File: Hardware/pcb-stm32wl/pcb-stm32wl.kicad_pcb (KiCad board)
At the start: 4 copper layers, 40.9 x 67.7 mm, 166 parts, among them J1 Debug, J2 U.FL-R-SMT-1, J3 Grove_I2C, Q1 SI2323DS, Q2 2SC4213, SW1 SW_Push, SW2 RESET, U1 TPS22917DBV, U10 NX3L1T3157GM, U11 BGS13S4N9, U12 NX3L1T3157GM, U2 RP605Z283B, U3 TPS22917DBV, U4 TPS22917DBV, U5 MX25R1635, U6 LIS2DH12, U7 SHTC3, U8 ATECC608A-TNGLORAU, U9 STM32WLxx_QFN48, X1 32MHz, X2 32.768KHz

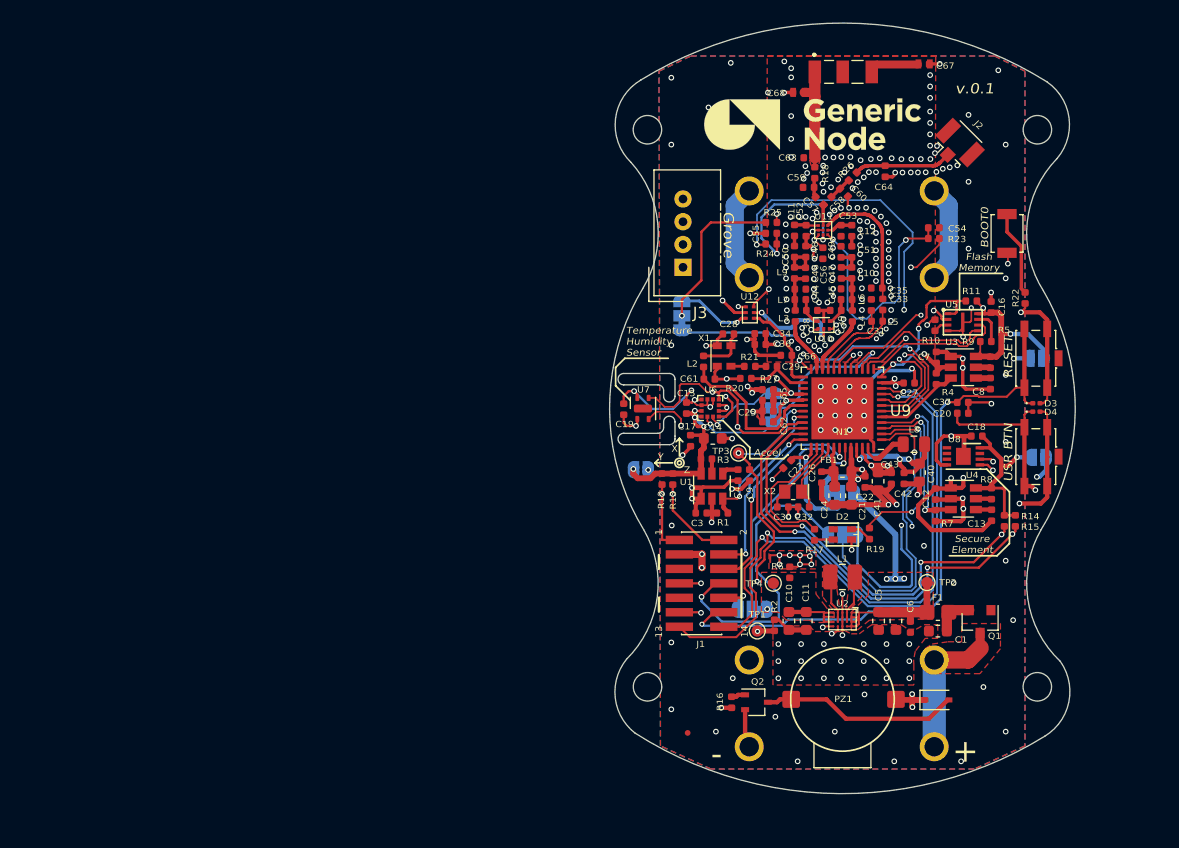
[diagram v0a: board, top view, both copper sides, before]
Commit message: pcb,sch: Add V0.2 HW design with external battery holder
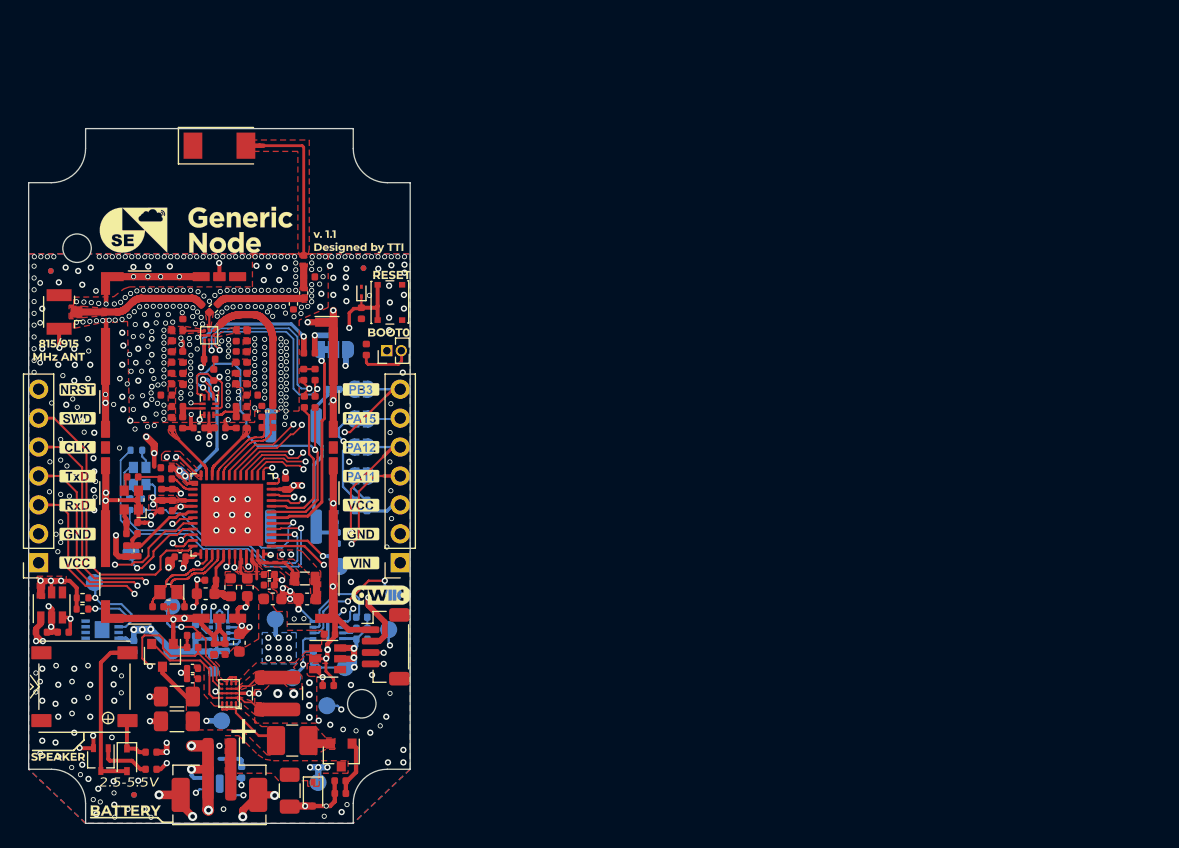
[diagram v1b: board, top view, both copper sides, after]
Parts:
- removed BH1, BH3: Battery_Cell+, node-lib-v1:BAT_BK-92
- removed BH2, BH4: Battery_Cell-, node-lib-v1:BAT_BK-92
- removed C51, C66: 33pF, Capacitor_SMD:C_0402_1005Metric
- removed C52: 2.7pF, Capacitor_SMD:C_0402_1005Metric
- removed C53: 1.3pF, Capacitor_SMD:C_0402_1005Metric
- removed C56: 1nF, Capacitor_SMD:C_0402_1005Metric
- removed C67: 5.0pF, Capacitor_SMD:C_0402_1005Metric
- removed C68: 3.6pF, Capacitor_SMD:C_0402_1005Metric
- removed G***: LOGO, node-lib-v1:qr_azerimaker_11mm
- removed G*** (x2): LOGO, node-lib-v1:Icon_Battery_1000px
- removed G*** (x2): LOGO, node-lib-v1:Logo_GN-4000px
- removed H3, H4: MountingHole, MountingHole:MountingHole_2.5mm
- removed JP10: BOOT0, Button_Switch_SMD:SW_SPST_B3U-1000P
- removed JP11: VDD_RF_SW, Jumper:SolderJumper-3_P1.3mm_Bridged12_RoundedPad1.0x1.5mm_NumberLabels
- removed JP7: VBAT, Jumper:SolderJumper-3_P1.3mm_Bridged12_RoundedPad1.0x1.5mm_NumberLabels
- removed JP8: SWO, Jumper:SolderJumper-3_P1.3mm_Bridged12_RoundedPad1.0x1.5mm_NumberLabels
- removed JP9: INT, Jumper:SolderJumper-3_P1.3mm_Bridged12_RoundedPad1.0x1.5mm_NumberLabels
- removed R25: 100R, Resistor_SMD:R_0402_1005Metric
- removed R26, R27: 0R, Resistor_SMD:R_0402_1005Metric
- removed the REF** at (139.7, 95.5)
- removed the REF** at (147.8, 95.5)
- removed U12: NX3L1T3157GM, node-lib-v1:6-XFDFN_SOT-886
- removed X2: 32.768KHz, node-lib-v1:Crystal_SMD_NX2012SA_32.768KHz
- added D5: ESD9D5V, Diode_SMD:D_SOD-923, F.Cu at (97.5, 88.8)
- added FID2: Fiducial, Fiducial:Fiducial_0.5mm_Mask1.5mm, B.Cu at (77.5, 133.0)
- added FID3: Fiducial, Fiducial:Fiducial_0.5mm_Mask1.5mm, F.Cu at (70.2, 87.0)
- added FID4: Fiducial, Fiducial:Fiducial_0.5mm_Mask1.5mm, B.Cu at (70.2, 87.0)
- added FID5: Fiducial, Fiducial:Fiducial_0.5mm_Mask1.5mm, F.Cu at (97.7, 86.8)
- added FID6: Fiducial, Fiducial:Fiducial_0.5mm_Mask1.5mm, B.Cu at (97.7, 86.8)
- added G-ACCELL: LOGO, node-lib-v1:LAbel_ACCELL_2000px, B.Cu at (83.1, 123.0)
- added G-ANT: LOGO, node-lib-v1:Label_ANT, F.Cu at (71.0, 93.9)
- added G-BAT: LOGO, node-lib-v1:Label_BATTERY_2500px, F.Cu at (76.7, 134.3)
- added G-BOOT0: LOGO, node-lib-v1:Label_BOOT0_4000px, F.Cu at (99.8, 92.3)
- added G-CLK: LOGO, node-lib-v1:PinName_CLK, F.Cu at (72.6, 102.5)
- added G-FLASH: LOGO, node-lib-v1:Label_FLASH_3000px, B.Cu at (92.3, 115.1)
- added G-GND: LOGO, node-lib-v1:PinName_GND, F.Cu at (97.4, 110.1)
- added G-GND2: LOGO, node-lib-v1:PinName_GND, F.Cu at (72.6, 110.1)
- added G-Logo: LOGO, node-lib-v1:Logo_GN-SE-4500px, F.Cu at (83.0, 83.4)
- added G-NRST: LOGO, node-lib-v1:PinName_NRST, F.Cu at (72.6, 97.4)
- added G-PA11: LOGO, node-lib-v1:PinName_PA11, F.Cu at (97.4, 105.0)
- added G-PA12: LOGO, node-lib-v1:PinName_PA12, F.Cu at (97.4, 102.5)
- added G-PA15: LOGO, node-lib-v1:PinName_PA15, F.Cu at (97.4, 99.9)
- added G-PB3: LOGO, node-lib-v1:PinName_PB3, F.Cu at (97.4, 97.4)
- added G-QWIIC: LOGO, node-lib-v1:Logo_qwiic_4000px, F.Cu at (99.2, 115.4)
- added G-RST: LOGO, node-lib-v1:Label_RESET_4000px, F.Cu at (100.1, 87.3)
- added G-RXD: LOGO, node-lib-v1:PinName_RxD, F.Cu at (72.6, 107.5)
- added G-SE: LOGO, node-lib-v1:Label_SE_3000px, B.Cu at (77.0, 115.0)
- added G-SPKR: LOGO, node-lib-v1:Label_Speaker, F.Cu at (70.9, 129.6)
- added G-SWD: LOGO, node-lib-v1:PinName_SWD, F.Cu at (72.6, 99.9)
- added G-TH: LOGO, node-lib-v1:Label_T_H_2000px, B.Cu at (90.0, 128.8)
- added G-TXD: LOGO, node-lib-v1:PinName_TxD, F.Cu at (72.6, 105.0)
- added G-VCC: LOGO, node-lib-v1:PinName_VCC, F.Cu at (97.4, 107.5)
- added G-VCC2: LOGO, node-lib-v1:PinName_VCC, F.Cu at (72.5, 112.6)
- added G-VIN: LOGO, node-lib-v1:PinName_VIN, F.Cu at (97.4, 112.6)
- added G-version: LOGO, node-lib-v1:Logo_design_version_2000px, F.Cu at (97.5, 84.2)
- added J10: Qwiic, Connector_JST:JST_SH_BM04B-SRSS-TB_1x04-1MP_P1.00mm_Vertical, F.Cu at (99.6, 120.0)
- added J4: RF_Shield_One_Piece, node-lib-v1:RF_Shield_SnapOn_30x20mm_w_Cutout_n_GND_Pads, F.Cu at (85.0, 102.5)
- added J5: S1001-46R, node-lib-v1:RF_Shield_Clip_S1001-46R, F.Cu at (85.0, 117.5)
- added J6: S1001-46R, node-lib-v1:RF_Shield_Clip_S1001-46R, F.Cu at (95.0, 102.5)
- added J7: U.FL/iPEX, Connector_Coaxial:U.FL_Hirose_U.FL-R-SMT-1_Vertical, F.Cu at (71.4, 90.6)
- added J8: DEBUG, Connector_PinSocket_2.54mm:PinSocket_1x07_P2.54mm_Vertical, F.Cu at (69.1, 112.6)
- added J9: UART/I2C, Connector_PinSocket_2.54mm:PinSocket_1x07_P2.54mm_Vertical, F.Cu at (100.9, 112.6)
- added JP4: SCL2_CUT, Jumper:SolderJumper-2_P1.3mm_Bridged2Bar_RoundedPad1.0x1.5mm, B.Cu at (97.4, 102.5)
- added JP5: BOOT0, Connector_PinHeader_1.27mm:PinHeader_1x02_P1.27mm_Vertical, F.Cu at (99.7, 94.0)
- added L13: 23nH, Inductor_SMD:L_0402_1005Metric, F.Cu at (92.4, 86.1)
- added L14: 4.3nH, Inductor_SMD:L_0402_1005Metric, F.Cu at (92.9, 87.5)
- added REF**: FabDrawing-4Layer, node-lib-v1:PCBStackup_FabDrawing-4Layer-Metric, F.Cu at (150.0, 72.5)
- added TP10: VCC_F, TestPoint:TestPoint_Pad_D1.5mm, B.Cu at (96.0, 121.8)
- added TP11: VCC_S, TestPoint:TestPoint_Pad_D1.5mm, B.Cu at (80.8, 120.4)
- added TP12: SDA, TestPoint:TestPoint_Pad_D1.5mm, B.Cu at (77.2, 111.7)
- added TP13: SCL, TestPoint:TestPoint_Pad_D1.5mm, B.Cu at (74.0, 114.4)
- added TP5: VCC, TestPoint:TestPoint_Pad_D1.5mm, B.Cu at (89.9, 117.6)
- added TP6: CS, TestPoint:TestPoint_Pad_D1.5mm, B.Cu at (91.4, 122.7)
- added TP7: MISO, TestPoint:TestPoint_Pad_D1.5mm, B.Cu at (100.3, 115.4)
- added TP8: SCK, TestPoint:TestPoint_Pad_D1.5mm, B.Cu at (94.4, 125.2)
- added TP9: MOSI, TestPoint:TestPoint_Pad_D1.5mm, B.Cu at (99.9, 118.5)
- added Y1: 32.768KHz, node-lib-v1:Crystal_SMD_NX2012SA_32.768KHz, F.Cu at (80.5, 115.2)
- AE1: value ANT_M620720 -> NN02-201; footprint node-lib-v1:ANT_M620720 -> node-lib-v1:Antenna_Fractus_NN02-201
- C1: value 10uF -> 100uF; footprint Capacitor_SMD:C_0603_1608Metric -> Capacitor_SMD:C_1206_3216Metric
- C10: value DNM -> 100nF; footprint Capacitor_SMD:C_0603_1608Metric -> Capacitor_SMD:C_0402_1005Metric
- C11: value 22uF -> 1uF; footprint Capacitor_SMD:C_0603_1608Metric -> Capacitor_SMD:C_0402_1005Metric
- C12: value 1uF -> 22uF; footprint Capacitor_SMD:C_0402_1005Metric -> Capacitor_SMD:C_0603_1608Metric
- C13: value DNM -> 4.7uF; footprint Capacitor_SMD:C_0402_1005Metric -> Capacitor_SMD:C_0603_1608Metric
- C14: value 10uF -> 100nF; footprint Capacitor_SMD:C_0603_1608Metric -> Capacitor_SMD:C_0402_1005Metric
- C15, C27: value 100nF -> 4.7uF; footprint Capacitor_SMD:C_0402_1005Metric -> Capacitor_SMD:C_0603_1608Metric
- C19, C22, C42: value 100nF -> 33pF
- C2: value 10uF -> 10nF; footprint Capacitor_SMD:C_0603_1608Metric -> Capacitor_SMD:C_0402_1005Metric
- C20: value DNM -> 100nF
- C21, C41: value 4.7uF -> 33pF; footprint Capacitor_SMD:C_0603_1608Metric -> Capacitor_SMD:C_0402_1005Metric
- C23: value 100nF -> 47pF
- C24: value 4.7uF -> 100nF; footprint Capacitor_SMD:C_0603_1608Metric -> Capacitor_SMD:C_0402_1005Metric
- C25: value 100nF -> 47nF
- C26: value 100nF -> 68pF
- C28: value 10nF -> 470nF; footprint Capacitor_SMD:C_0402_1005Metric -> Capacitor_SMD:C_0603_1608Metric
- C29: value 1nF -> 100nF
- C30, C44: value 6.8pF -> 2.7pF
- C31: value 2.7pF -> 3.6pF
- C32: value 6.8pF -> 33pF
- C33: value 3.6pF -> 33pF
- C34: value 47nF -> 10nF
- C35: value DNM -> 5.6pF
- C36: value 68nF -> 6.8pF
- C37: value 100nF -> 2.7pF
- C38: value 33pF -> 2.4pF
- C39: value 33pF -> 3.3pF
- C4: value DNM -> 100uF; footprint Capacitor_SMD:C_0402_1005Metric -> Capacitor_SMD:C_1206_3216Metric
- C40: value 470nF -> 3.9pF; footprint Capacitor_SMD:C_0603_1608Metric -> Capacitor_SMD:C_0402_1005Metric
- C43: value 100nF -> 1nF
- C45: value 5.6pF -> 1.3pF
- C46: value 2.4pF -> 5.6pF
- C47: value 2.7pF -> 1nF
- C48: value 3.9pF -> 1nF
- C49: value 3.3pF -> 5.6pF
- C5: value 4.7uF -> 100uF; footprint Capacitor_SMD:C_0603_1608Metric -> Capacitor_SMD:C_1206_3216Metric
- C50: value 33pF -> 1nF
- C54: value 1nF -> 3.3pF
- C55: value 1nF -> DNM
- C57, C65: value 33pF -> 100nF
- C58: value DNM -> 10uF; footprint Capacitor_SMD:C_0402_1005Metric -> Capacitor_SMD:C_0603_1608Metric; moved to B.Cu
- C59, C60, C63, C64: value DNM -> 100nF; moved to B.Cu
- C6: value 100nF -> 1uF
- C61, R15, R24: moved to B.Cu
- C62: value 33pF -> 100nF; moved to B.Cu
- C7: value 1uF -> 100nF
- C8: value DNM -> 1uF
- D1: value 1N4148WS -> PESD5V0S1BA
- D2: value EAST1616RGBB2 -> 1N4148WSF-7; footprint node-lib-v1:LED_RGB_0606 -> node-lib-v1:D_SOD-323F_custom
- D3: value ESDALC6V1-1U2 -> FM-B2020RGBA; footprint Diode_SMD:D_0201_0603Metric -> LED_SMD:LED_Cree-PLCC4_2x2mm_CW; moved to B.Cu
- D4: value ESDALC6V1-1U2 -> ESD9D5V; footprint Diode_SMD:D_0201_0603Metric -> Diode_SMD:D_SOD-923; moved to B.Cu
- F1: value PTC 6V 750MA -> PTC 13V 1A; footprint node-lib-v1:Fuse_0805_2012Metric_Castellated -> Fuse:Fuse_1210_3225Metric_Castellated
- J1: value Debug -> S1001-46R; footprint node-lib-v1:PinHeader_2x07_P1.27mm_Vertical_SMD -> node-lib-v1:RF_Shield_Clip_S1001-46R
- J2: value U.FL-R-SMT-1 -> JST-PH; footprint Connector_Coaxial:U.FL_Hirose_U.FL-R-SMT-1_Vertical -> Connector_JST:JST_PH_B2B-PH-SM4-TB_1x02-1MP_P2.00mm_Vertical
- J3: value Grove_I2C -> S1001-46R; footprint Connector:NS-Tech_Grove_1x04_P2mm_Vertical -> node-lib-v1:RF_Shield_Clip_S1001-46R
- JP1: value Sensor_VCC -> VDD_RF_SW; footprint Jumper:SolderJumper-2_P1.3mm_Open_RoundedPad1.0x1.5mm -> Jumper:SolderJumper-3_P1.3mm_Bridged12_RoundedPad1.0x1.5mm_NumberLabels
- JP2: value Flash_VCC -> BUZZ_KILL; footprint Jumper:SolderJumper-2_P1.3mm_Open_RoundedPad1.0x1.5mm -> Jumper:SolderJumper-2_P1.3mm_Bridged2Bar_RoundedPad1.0x1.5mm
- JP3: value Secure_Element_VCC -> SDA2_CUT; footprint Jumper:SolderJumper-2_P1.3mm_Open_RoundedPad1.0x1.5mm -> Jumper:SolderJumper-2_P1.3mm_Bridged2Bar_RoundedPad1.0x1.5mm
- JP6: value JTDI -> BTN_CUT; footprint Jumper:SolderJumper-3_P1.3mm_Bridged12_RoundedPad1.0x1.5mm_NumberLabels -> Jumper:SolderJumper-2_P1.3mm_Bridged2Bar_RoundedPad1.0x1.5mm
- L1: value 2.2 uH -> 2.2uH; footprint Inductor_SMD:L_1008_2520Metric -> node-lib-v1:L_HPC4012TF-2R2M
- L10: value 3.3nH -> 1400R @1GHz
- L2: value 1400R @1GHz -> 3.3nH
- L4: value 3.3nH -> 15uH; footprint Inductor_SMD:L_0402_1005Metric -> node-lib-v1:L_0805_2012Metric_custom
- L8: value 15uH -> 3nH; footprint Inductor_SMD:L_0805_2012Metric -> Inductor_SMD:L_0402_1005Metric
- N1: value NewAge_3inch_round -> BoLink-16174563; footprint node-lib-v1:NewAge_3inch_round -> node-lib-v1:BoLink_704025
- PZ1: value AST0927 2.73kHz 85dB -> MLT-7525; footprint node-lib-v1:Buzzer_AST0927MW-3.6TRQ -> node-lib-v1:Buzzer_MLT-7525
- Q1: value SI2323DS -> CEN2321A
- Q2: value 2SC4213 -> S9013W
- R1: value 100K -> 10K
- R11: value 10K -> DNM; moved to B.Cu
- R12: value 4K7 -> DNM; moved to B.Cu
- R13: value 4K7 -> 10K; moved to B.Cu
- R17: value 330R -> 4K7
- R18: value 0R -> 4K7; moved to B.Cu
- R19: value 100R -> 33R
- R20: value DNM -> 10K
- R21: value 220R -> 1K; footprint Inductor_SMD:L_0402_1005Metric -> Resistor_SMD:R_0402_1005Metric; moved to B.Cu
- R22: value 10K -> 330R; footprint Inductor_SMD:L_0402_1005Metric -> Resistor_SMD:R_0402_1005Metric; moved to B.Cu
- R23: value 100R -> 330R; moved to B.Cu
- R3: value 1K -> 100K
- R5: value 1K -> 220R; footprint Resistor_SMD:R_0402_1005Metric -> Inductor_SMD:L_0402_1005Metric
- R6: value 0R -> 100R
- R7: value 100K -> 100R
- R8: value 1K -> 100R
- R9: value DNM -> 0R
- SW1: value SW_Push -> USR_BTN; footprint node-lib-v1:EVQ-P2R02W -> node-lib-v1:PushButton_KSC721GLFS; moved to B.Cu
- SW2: footprint node-lib-v1:EVQ-P2R02W -> node-lib-v1:SW_SPST_SKSHABE010
- TP1: value VBAT_READ -> VIN; footprint TestPoint:TestPoint_Pad_D1.0mm -> TestPoint:TestPoint_Pad_D1.5mm; moved to B.Cu
- TP2: footprint TestPoint:TestPoint_Pad_D1.0mm -> TestPoint:TestPoint_Pad_D1.5mm; moved to B.Cu
- TP3: value VBAT_ADC -> VBAT_READ_EN; footprint TestPoint:TestPoint_Pad_D1.0mm -> TestPoint:TestPoint_Pad_D1.5mm; moved to B.Cu
- TP4: value VDD -> VBAT_ADC; footprint TestPoint:TestPoint_Pad_D1.0mm -> TestPoint:TestPoint_Pad_D1.5mm; moved to B.Cu
- U10: value NX3L1T3157GM -> SHTC3; footprint node-lib-v1:6-XFDFN_SOT-886 -> node-lib-v1:Sensirion_DFN-4-1EP_2x2mm_P1mm_EP0.7x1.6mm; moved to B.Cu
- U11: value BGS13S4N9 -> ATECC608A-TNGLORA; footprint node-lib-v1:RFSW_BGS13S4N9E6327XTSA1 -> Package_DFN_QFN:DFN-8-1EP_3x2mm_P0.5mm_EP1.3x1.5mm; moved to B.Cu
- U2: value RP605Z283B -> TPS3839G25; footprint node-lib-v1:WLCSP-20-P3_1.994x1.609mm_Layout5x4_P0.4mm -> Package_TO_SOT_SMD:SOT-23
- U4: value TPS22917DBV -> RP605Z283B; footprint Package_TO_SOT_SMD:SOT-23-6 -> node-lib-v1:WLCSP-20-P3_1.994x1.609mm_Layout5x4_P0.4mm
- U5: value MX25R1635 -> STM32WLE5CC; footprint node-lib-v1:FLASH_UFDFN-8-MX25R1635F -> Package_DFN_QFN:QFN-48-1EP_7x7mm_P0.5mm_EP5.45x5.45mm
- U6: value LIS2DH12 -> TS3A5223RSWR; footprint Package_LGA:LGA-12_2x2mm_P0.5mm -> Package_DFN_QFN:UQFN-10_1.4x1.8mm_P0.4mm
- U7: value SHTC3 -> BGS13S4N9; footprint node-lib-v1:Sensirion_DFN-4-1EP_2x2mm_P1mm_EP0.7x1.6mm -> node-lib-v1:RFSW_BGS13S4N9E6327XTSA1
- U8: value ATECC608A-TNGLORAU -> MX25R1635; footprint Package_DFN_QFN:DFN-8-1EP_3x2mm_P0.5mm_EP1.3x1.5mm -> node-lib-v1:FLASH_UFDFN-8-MX25R1635F; moved to B.Cu
- U9: value STM32WLxx_QFN48 -> LIS2DH12; footprint Package_DFN_QFN:QFN-48-1EP_7x7mm_P0.5mm_EP5.45x5.45mm -> Package_LGA:LGA-12_2x2mm_P0.5mm; moved to B.Cu
- X1: footprint node-lib-v1:TCXO_NT2016SA-32M-END4263A -> Crystal:Crystal_SMD_Abracon_ABM10-4Pin_2.5x2.0mm
- moved J2 85.0 mm to (85.0, 131.2), turned to 180 degrees
- moved R14 81.2 mm to (73.0, 115.7), turned to 180 degrees
- moved R22 79.2 mm to (77.7, 102.7), turned to 0 degrees
- moved D3 79.0 mm to (78.0, 105.0), turned to 270 degrees
- moved R5 76.0 mm to (77.4, 105.1), turned to 180 degrees
- moved C16 74.5 mm to (81.5, 112.1), turned to 180 degrees
- moved C63 73.4 mm to (87.0, 131.0), turned to 270 degrees
- moved R23 73.4 mm to (78.2, 107.5), turned to 90 degrees
- moved U11 72.4 mm to (74.7, 118.5), turned to 0 degrees
- moved C18 71.8 mm to (79.9, 106.6), turned to 90 degrees
- moved C7 71.1 mm to (82.6, 122.8), turned to 180 degrees
- moved R9 67.9 mm to (84.5, 90.3), turned to 225 degrees
- moved C58 67.5 mm to (84.5, 121.4), turned to 90 degrees
- moved L10 67.2 mm to (77.3, 110.1), turned to 180 degrees
- moved U4 66.7 mm to (85.8, 124.1), turned to 90 degrees
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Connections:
- AE1 pad 1: Net-(AE1-Pad1) -> (no net)
- C1 pad 2: Net-(C1-Pad2) -> Vin
- C10 pad 2: Net-(C10-Pad2) -> VDDRF
- C11 pad 1: GND -> VDDRF
- C11 pad 2: Net-(C10-Pad2) -> GND
- C12 pad 1: VDD -> GND
- C12 pad 2: GND -> VDDRF
- C13 pad 1: VDD -> VDDRF
- C13 pad 2: Net-(C13-Pad2) -> GND
- C14 pad 1: GND -> VDDRF
- C14 pad 2: /Peripherals/VCC_SENSORS -> GND
- C15 pad 1: GND -> VDDA
- C15 pad 2: /Peripherals/VCC_SENSORS -> GND
- C16 pad 1: GND -> VDDRF
- C16 pad 2: /Peripherals/VCC_FLASH -> GND
- C17 pad 1: GND -> VDDA
- C17 pad 2: /Peripherals/VCC_SENSORS -> GND
- C18 pad 1: GND -> VDDRF
- C18 pad 2: /Peripherals/VCC_SEC_ELM -> GND
- C19 pad 1: GND -> VDDRF
- C19 pad 2: /Peripherals/VCC_SENSORS -> GND
- C2 pad 1: GND -> Net-(C2-Pad1)
- C2 pad 2: +BATT -> GND
- C20 pad 1: GND -> VDDRF
- C20 pad 2: /LoRa MCU/PB3 -> GND
- C21 pad 1: VDD -> VDDPA
- C22 pad 1: VDD -> VDDRF1V55
- C23 pad 1: Net-(C23-Pad1) -> PB0_VDD_TCXO
- C24 pad 1: VDDA -> PB0_VDD_TCXO
- C25 pad 1: VDDRF -> GND
- C25 pad 2: GND -> Net-(C25-Pad2)
- C26 pad 1: VDDA -> Net-(C25-Pad2)
- C27 pad 1: VDD -> VDDRF
- C28 pad 1: GND -> VDDRF1V55
- C28 pad 2: Net-(C28-Pad2) -> GND
- C29 pad 1: Net-(C29-Pad1) -> VDDRF
- C29 pad 2: OSC_IN -> GND
- C3 pad 1: VDD -> VDDRF
- C30 pad 2: OSC32_IN -> /LoRa MCU/RFI_N
- C31 pad 1: GND -> /LoRa MCU/RFI_P
- C32 pad 2: OSC32_OUT -> Net-(C32-Pad2)
- C33 pad 1: /LoRa MCU/RFI_P -> Net-(C33-Pad1)
- C33 pad 2: Net-(C33-Pad2) -> GND
- C35 pad 1: Net-(C33-Pad2) -> GND
- C35 pad 2: GND -> Net-(C35-Pad2)
- C36 pad 1: Net-(C34-Pad2) -> GND
- C36 pad 2: GND -> Net-(C36-Pad2)
- C37 pad 1: GND -> Net-(C35-Pad2)
- C37 pad 2: NRST -> Net-(C37-Pad2)
- C38 pad 1: GND -> Net-(C36-Pad2)
- C39 pad 1: Net-(C39-Pad1) -> GND
- C39 pad 2: GND -> Net-(C37-Pad2)
- C4 pad 1: VDD -> GND
- C4 pad 2: Net-(C4-Pad2) -> +BATT
- C40 pad 1: VDDRF1V55 -> GND
- C40 pad 2: GND -> Net-(C38-Pad2)
- C41 pad 1: VDDRF -> Net-(C38-Pad2)
- C41 pad 2: GND -> Net-(C41-Pad2)
- C42 pad 1: VDDRF1V55 -> Net-(C37-Pad2)
- C42 pad 2: GND -> Net-(C42-Pad2)
- C43 pad 1: VDDRF -> Net-(C43-Pad1)
- C43 pad 2: GND -> OSC_IN
- C46 pad 1: Net-(C44-Pad2) -> GND
- C46 pad 2: Net-(C46-Pad2) -> OSC32_IN
- C47 pad 1: Net-(C45-Pad2) -> GND
- C48 pad 2: Net-(C46-Pad2) -> Net-(C48-Pad2)
- C49 pad 2: Net-(C47-Pad2) -> OSC32_OUT
- C5 pad 1: +BATT -> GND
- C5 pad 2: GND -> +BATT
- C50 pad 1: Net-(C46-Pad2) -> GND
- C54 pad 1: GND -> Net-(C54-Pad1)
- C55 pad 2: Net-(C55-Pad2) -> Net-(C54-Pad2)
- C57 pad 1: Net-(C57-Pad1) -> VDDRF
- C57 pad 2: Net-(C57-Pad2) -> GND
- C58 pad 1: Net-(C57-Pad1) -> GND
- C58 pad 2: Net-(C58-Pad2) -> /Peripherals/VCC_SENSORS
- C59 pad 2: Net-(C57-Pad2) -> /Peripherals/VCC_SENSORS
- C60 pad 2: Net-(C58-Pad2) -> /Peripherals/VCC_FLASH
- C61 pad 1: PB0_VDD_TCXO -> GND
- C61 pad 2: GND -> /Peripherals/VCC_SENSORS
- C62 pad 1: VDDRF1V55 -> GND
- C62 pad 2: GND -> /Peripherals/VCC_SENSORS
- C63 pad 2: Net-(AE1-Pad1) -> /Peripherals/VCC_SENSORS
- C65 pad 1: VDDRF -> GND
- C65 pad 2: GND -> /LoRa MCU/NRST
- C7 pad 1: VDD -> +BATT
- C8 pad 1: VDD -> VDDRF
- C8 pad 2: Net-(C8-Pad2) -> GND
- D1 pad 1: VDD -> Vin
- D1 pad 2: Net-(D1-Pad2) -> GND
- D3 pad 1: NRST -> Net-(D3-Pad1)
- D3 pad 2: GND -> Net-(D3-Pad2)
- D4 pad 1: /LoRa MCU/PB3 -> Net-(C64-Pad2)
- F1 pad 2: Net-(C1-Pad2) -> Net-(F1-Pad2)
- FB1 pad 2: VDD -> VDDRF
- J1 pad 1: /LoRa MCU/I2C1_SDA -> GND
- J2 pad 1: Net-(C64-Pad2) -> Vin
- J3 pad 1: /LoRa MCU/I2C1_SCL -> GND
- JP1 pad 1: VDD -> FE_CTRL3
- JP1 pad 2: /Peripherals/VCC_SENSORS -> Net-(JP1-Pad2)
- JP2 pad 1: VDD -> /LoRa MCU/PA15
- JP2 pad 2: /Peripherals/VCC_FLASH -> Net-(JP2-Pad2)
- JP3 pad 1: VDD -> Net-(JP3-Pad1)
- JP3 pad 2: /Peripherals/VCC_SEC_ELM -> /LoRa MCU/PA11_SDA2
- JP6 pad 1: /Peripherals/BUZZER -> /LoRa MCU/PB3
- L10 pad 1: Net-(C45-Pad2) -> PB0_VDD_TCXO
- L10 pad 2: Net-(C47-Pad2) -> Net-(C34-Pad2)
- L11 pad 1: Net-(C50-Pad2) -> Net-(C41-Pad2)
- L11 pad 2: Net-(C52-Pad2) -> Net-(C44-Pad2)
- L12 pad 1: Net-(C51-Pad2) -> Net-(C42-Pad2)
- L12 pad 2: Net-(C53-Pad2) -> Net-(C45-Pad2)
- L2 pad 1: PB0_VDD_TCXO -> Net-(L2-Pad1)
- L2 pad 2: Net-(C28-Pad2) -> Net-(C35-Pad2)
- L3 pad 2: Net-(C44-Pad2) -> Net-(C36-Pad2)
- L4 pad 1: Net-(L4-Pad1) -> VLXSMPS
- L4 pad 2: Net-(C45-Pad2) -> VDDRF1V55
- L5 pad 1: Net-(C31-Pad2) -> /LoRa MCU/RFI_N
- L6 pad 1: Net-(C39-Pad1) -> Net-(C32-Pad2)
- L6 pad 2: Net-(C45-Pad2) -> Net-(C36-Pad2)
- L7 pad 1: Net-(C38-Pad2) -> Net-(C33-Pad1)
- L7 pad 2: Net-(C44-Pad2) -> Net-(C35-Pad2)
- L8 pad 1: VLXSMPS -> Net-(C35-Pad2)
- L8 pad 2: VDDRF1V55 -> Net-(C37-Pad2)
- L9 pad 1: Net-(C44-Pad2) -> Net-(C36-Pad2)
- L9 pad 2: Net-(C46-Pad2) -> Net-(C38-Pad2)
- PZ1 pad 1: VDD -> Net-(D2-Pad1)
- PZ1 pad 2: Net-(D1-Pad2) -> Net-(D2-Pad2)
- Q1 pad 1: GND -> Net-(C2-Pad1)
- Q1 pad 2: Net-(C1-Pad2) -> Net-(F1-Pad2)
- Q1 pad 3: Net-(BH1-Pad1) -> Vin
- Q2 pad 3: Net-(D1-Pad2) -> Net-(D2-Pad2)
- R1 pad 2: /LoRa MCU/PB12 -> Net-(C2-Pad1)
- R10 pad 1: /Peripherals/VCC_FLASH -> Net-(J7-Pad1)
- R11 pad 2: /Peripherals/FlashCS -> Net-(R11-Pad2)
- R12 pad 1: /LoRa MCU/I2C1_SDA -> /Peripherals/VCC_FLASH
- R12 pad 2: /Peripherals/VCC_SENSORS -> Net-(R12-Pad2)
- R13 pad 1: /Peripherals/VCC_SENSORS -> /Peripherals/VCC_FLASH
- R13 pad 2: /LoRa MCU/I2C1_SCL -> /Peripherals/FlashCS
- R14 pad 1: /LoRa MCU/I2C2_SCL -> /LoRa MCU/PA09_SCL1
- R14 pad 2: /Peripherals/VCC_SEC_ELM -> /Peripherals/VCC_SENSORS
- R15 pad 1: /Peripherals/VCC_SEC_ELM -> Net-(JP3-Pad1)
- R15 pad 2: /LoRa MCU/I2C2_SDA -> VDDRF
- R16 pad 1: /Peripherals/BUZZER -> Net-(JP2-Pad2)
- R17 pad 1: Net-(D2-Pad1) -> /Peripherals/VCC_SENSORS
- R17 pad 2: /Peripherals/LED_R -> /LoRa MCU/PA10_SDA1
- R18 pad 1: Net-(AE1-Pad1) -> VDDRF
- R18 pad 2: Net-(C57-Pad2) -> Net-(JP4-Pad1)
- R19 pad 1: Net-(D2-Pad3) -> VDDRF
- R19 pad 2: /Peripherals/LED_B -> Net-(D2-Pad1)
- R2 pad 2: /LoRa MCU/PB4 -> /Power Supply/LS1_SENSORS_EN
- R20 pad 1: OSC_IN -> GND
- R20 pad 2: GND -> /LoRa MCU/BOOT0
- R21 pad 1: Net-(C29-Pad1) -> /LoRa MCU/PB5
- R21 pad 2: Net-(R21-Pad2) -> Net-(D3-Pad1)
- R22 pad 1: GND -> /LoRa MCU/PB6
- R22 pad 2: Net-(JP10-Pad2) -> Net-(D3-Pad4)
- R23 pad 1: Net-(C54-Pad2) -> /LoRa MCU/PB7
- R23 pad 2: FE_CTRL1 -> Net-(D3-Pad2)
- R24 pad 1: Net-(C55-Pad2) -> Net-(JP6-Pad2)
- R24 pad 2: FE_CTRL2 -> Net-(C64-Pad2)
- R3 pad 1: /Peripherals/VCC_SENSORS -> GND
- R3 pad 2: Net-(R3-Pad2) -> /LoRa MCU/PB4
- R4 pad 2: /LoRa MCU/PB7 -> /Power Supply/LS2_FLASH_EN
- R5 pad 1: /Peripherals/VCC_FLASH -> Net-(C43-Pad1)
- R6 pad 1: Net-(C10-Pad2) -> Net-(C47-Pad2)
- R6 pad 2: VDD -> FE_CTRL2
- R7 pad 1: GND -> Net-(C48-Pad2)
- R7 pad 2: /LoRa MCU/PB6 -> FE_CTRL1
- R8 pad 1: /Peripherals/VCC_SEC_ELM -> Net-(JP1-Pad2)
- R8 pad 2: Net-(R8-Pad2) -> Net-(C50-Pad2)
- R9 pad 1: /Peripherals/VCC_FLASH -> Net-(C54-Pad2)
- R9 pad 2: Net-(R9-Pad2) -> Net-(R10-Pad2)
- SW1 pad 1: GND -> Net-(C64-Pad2)
- SW1 pad 2: /LoRa MCU/PB3 -> GND
- SW2 pad 2: NRST -> /LoRa MCU/NRST
- TP1 pad 1: /LoRa MCU/PB4 -> Vin
- TP3 pad 1: /LoRa MCU/PB2 -> /LoRa MCU/PB4
- TP4 pad 1: Net-(C10-Pad2) -> /LoRa MCU/PB2
- U1 pad 1: VDD -> VDDRF
- U1 pad 3: /LoRa MCU/PB12 -> /Power Supply/LS1_SENSORS_EN
- U1 pad 4: Net-(C4-Pad2) -> (no net)
- U1 pad 5: Net-(R3-Pad2) -> /Peripherals/VCC_SENSORS
- U10 pad 1: Net-(C39-Pad1) -> /Peripherals/VCC_SENSORS
- U10 pad 2: GND -> /LoRa MCU/PA09_SCL1
- U10 pad 3: Net-(C38-Pad2) -> /LoRa MCU/PA10_SDA1
- U10 pad 4: Net-(C34-Pad2) -> GND
- U10 pad 5: VDD -> (no net)
- U11 pad 1: Net-(C54-Pad2) -> (no net)
- U11 pad 2: Net-(C53-Pad2) -> (no net)
- U11 pad 3: Net-(C33-Pad2) -> (no net)
- U11 pad 4: Net-(C57-Pad1) -> GND
- U11 pad 5: Net-(C52-Pad2) -> /LoRa MCU/PA10_SDA1
- U11 pad 6: GND -> /LoRa MCU/PA09_SCL1
- U11 pad 7: Net-(C56-Pad2) -> (no net)
- U11 pad 8: Net-(C55-Pad2) -> /Peripherals/VCC_SENSORS
- U3 pad 1: VDD -> VDDRF
- U3 pad 3: /LoRa MCU/PB7 -> /Power Supply/LS2_FLASH_EN
- U3 pad 4: Net-(C8-Pad2) -> (no net)
- U3 pad 5: Net-(R5-Pad2) -> /Peripherals/VCC_FLASH
- U5 pad 1: /Peripherals/FlashCS -> /LoRa MCU/PB3
- U5 pad 2: /Peripherals/MISO -> /LoRa MCU/PB4
- U5 pad 3: Net-(R10-Pad2) -> /LoRa MCU/PB5
- U5 pad 4: GND -> /LoRa MCU/PB6
- U5 pad 5: /Peripherals/MOSI -> /LoRa MCU/PB7
- U5 pad 6: /Peripherals/SCLK -> FE_CTRL3
- U5 pad 7: Net-(R9-Pad2) -> FE_CTRL1
- U5 pad 8: /Peripherals/VCC_FLASH -> FE_CTRL2
- U5 pad 9: GND -> /LoRa MCU/PA2_TxD2
- U6 pad 1: /LoRa MCU/I2C1_SCL -> VDDRF
- U6 pad 10: /Peripherals/VCC_SENSORS -> Net-(C33-Pad1)
- U6 pad 2: /Peripherals/VCC_SENSORS -> VDDRF1V55
- U6 pad 3: /Peripherals/VCC_SENSORS -> VDDPA
- U6 pad 4: /LoRa MCU/I2C1_SDA -> FE_CTRL1
- U6 pad 5: GND -> VDDRF
- U6 pad 7: GND -> Net-(C32-Pad2)
- U6 pad 8: GND -> FE_CTRL1
- U6 pad 9: /Peripherals/VCC_SENSORS -> Net-(C25-Pad2)
- U7 pad 1: /Peripherals/VCC_SENSORS -> Net-(C48-Pad2)
- U7 pad 2: /LoRa MCU/I2C1_SCL -> Net-(C45-Pad2)
- U7 pad 3: /LoRa MCU/I2C1_SDA -> Net-(C31-Pad2)
- U7 pad 4: GND -> Net-(R10-Pad2)
- U7 pad 5: Net-(U7-Pad5) -> Net-(C44-Pad2)
- U8 pad 1: (no net) -> /Peripherals/FlashCS
- U8 pad 2: (no net) -> /Peripherals/MISO
- U8 pad 3: (no net) -> Net-(R12-Pad2)
- U8 pad 5: /LoRa MCU/I2C2_SDA -> /Peripherals/MOSI
- U8 pad 6: /LoRa MCU/I2C2_SCL -> /LoRa MCU/PA5_SCK1
- U8 pad 7: (no net) -> Net-(R11-Pad2)
- U8 pad 8: /Peripherals/VCC_SEC_ELM -> /Peripherals/VCC_FLASH
- U9 pad 1: Net-(JP8-Pad2) -> /LoRa MCU/PA09_SCL1
- U9 pad 10: /LoRa MCU/USART2_RxD -> /Peripherals/VCC_SENSORS
- U9 pad 11: VDD -> /LoRa MCU/PA8
- U9 pad 12: /Peripherals/FlashCS -> (no net)
- U9 pad 2: /LoRa MCU/PB4 -> /Peripherals/VCC_SENSORS
- U9 pad 3: /Peripherals/LED_B -> /Peripherals/VCC_SENSORS
- U9 pad 4: /LoRa MCU/PB6 -> /LoRa MCU/PA10_SDA1
- U9 pad 5: /LoRa MCU/PB7 -> GND
- U9 pad 6: FE_CTRL3 -> GND
- U9 pad 7: FE_CTRL1 -> GND
- U9 pad 8: FE_CTRL2 -> GND
- U9 pad 9: /LoRa MCU/USART2_TxD -> /Peripherals/VCC_SENSORS
- X1 pad 3: Net-(R21-Pad2) -> Net-(R5-Pad2)
- X1 pad 4: Net-(C28-Pad2) -> Net-(C34-Pad2)
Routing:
- net VDD: track 179.8 -> 0.00 mm, vias 29 -> 0
- net VDDRF: track 46.7 -> 166.3 mm, vias 5 -> 22
- net /LoRa MCU/PA09_SCL1: track 0.00 -> 72.8 mm, vias 0 -> 5
- net /LoRa MCU/I2C1_SCL: track 69.9 -> 0.00 mm, vias 4 -> 0
- net NRST: track 69.3 -> 0.00 mm, vias 3 -> 0
- net /LoRa MCU/PA12_SCL2: track 0.00 -> 57.1 mm, vias 0 -> 3
- net /LoRa MCU/NRST: track 0.00 -> 56.6 mm, vias 0 -> 2
- net /LoRa MCU/USART2_TxD: track 54.2 -> 0.00 mm, vias 2 -> 0
- net /LoRa MCU/I2C1_SDA: track 53.2 -> 0.00 mm, vias 3 -> 0
- net Net-(BH2-Pad1): track 51.8 -> 0.00 mm
- net /LoRa MCU/PA10_SDA1: track 0.00 -> 51.2 mm, vias 0 -> 4
- net Net-(JP2-Pad2): track 0.00 -> 50.6 mm, vias 0 -> 3
- net /LoRa MCU/USART2_RxD: track 50.5 -> 0.00 mm, vias 2 -> 0
- net /LoRa MCU/PA11_SDA2: track 0.00 -> 50.4 mm, vias 0 -> 3
- net /LoRa MCU/I2C2_SDA: track 48.5 -> 0.00 mm, vias 4 -> 0
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- added copper zone on F.Cu, net /Peripherals/VCC_SENSORS
- added copper zone on In1.LF, net GND
- added copper zone on In2.PWR, net GND
- added copper zone on F.Cu, net Net-(AE1-Pad2)
- added copper zone on F.Cu, net Net-(C25-Pad2)
- added copper zone on F.Cu, net Net-(C31-Pad2)
- added copper zone on F.Cu, net Net-(C35-Pad2)
- added copper zone on F.Cu, net Net-(C36-Pad2)
- added copper zone on F.Cu, net Net-(C37-Pad2)
- added copper zone on F.Cu, net Net-(C38-Pad2)
- added copper zone on F.Cu, net Net-(C41-Pad2)
- added copper zone on F.Cu, net Net-(C42-Pad2)
- added copper zone on F.Cu, net Net-(C44-Pad2)
- added copper zone on F.Cu, net Net-(C45-Pad2)
- added copper zone on F.Cu, net Net-(C54-Pad1)
- added copper zone on F.Cu, net Net-(C54-Pad2)
- added copper zone on F.Cu, net Net-(F1-Pad2)
- added copper zone on F.Cu, net Net-(J7-Pad1)
- added copper zone on F.Cu, net Net-(L2-Pad1)
- added copper zone on F.Cu, net Net-(L3-Pad1)
- added copper zone on F.Cu, net Net-(R10-Pad2)
- added copper zone on F.Cu, net VDDPA
- added copper zone on B.Cu, net VDDRF
- added copper zone on F.Cu, net VDDRF
- added copper zone on In2.PWR, net VDDRF
- added copper zone on F.Cu, net VDDRF1V55
- added copper zone on F.Cu, net VLXSMPS
- added copper zone on F.Cu, net Vin
- removed copper zone on In1.GND, net GND
- removed copper zone on F.Cu, net Net-(AE1-Pad1)
- removed copper zone on F.Cu, net Net-(BH1-Pad1)
- removed copper zone on In2.PWR, net Net-(BH2-Pad1)
- removed copper zone on F.Cu, net Net-(C10-Pad2)
- removed copper zone on F.Cu, net VDD
- removed copper zone on In2.PWR, net VDD
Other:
- board size 40.9 x 67.7 mm -> 33.5 x 61 mm
- rule pad_to_mask_clearance: 0.05 -> 0
- rule trace_min: 0.127 -> 0.1
- rule via_min_drill: 0.2 -> 0.3
- board text added: "1. Material: 2. Soldermask color: 3. Silkscreen color: 4. Surface Finish: 5. Impedance Control: 6. VIAs: 7. Stackup:"
- board text added: "2.5-5.5V"
- board text added: "BUTTON"
- board text added: "CLK"
- board text added: "FR-4 (TG-150) Black/Blue White ENIG Yes Tented with soldermask See stackup table below for layer specific info"
- board text added: "GND"
- board text added: "LED"
- board text added: "NRST"
- board text added: "PA11"
- board text added: "PA12"
- board text added: "PA15"
- board text added: "PB3"
- board text added: "RXD"
- board text added: "SWD"
- board text added: "TXD"
- board text added: "VCC"
- board text added: "VIN"
- board text added: "~PCB Specifications"
- board text removed: "-"
- board text removed: "1.5V-AA"
- board text removed: "Accel."
- board text removed: "BOOT0"
- board text removed: "Flash Memory"
- board text removed: "Grove"
- board text removed: "RESET"
- board text removed: "Secure Element"
- board text removed: "Temperature Humidity Sensor"
- board text removed: "USR BTN"
- board text removed: "v.0.1"

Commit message: hw: Migrate sch and pcb files to KiCad v6
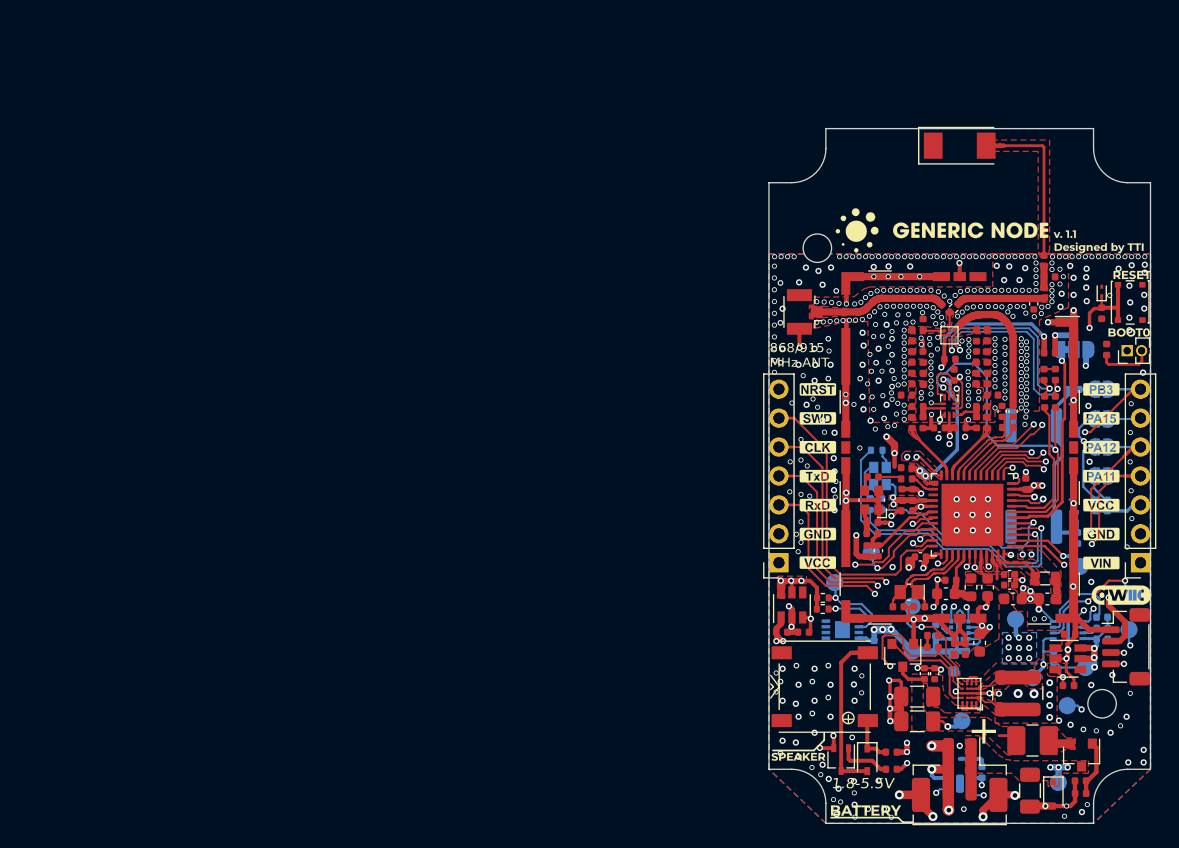
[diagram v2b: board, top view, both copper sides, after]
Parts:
- removed C54: 3.3pF, Capacitor_SMD:C_0402_1005Metric
- removed FID1, FID2, FID3, FID4, FID5, FID6: Fiducial, Fiducial:Fiducial_0.5mm_Mask1.5mm
- removed G-ANT: LOGO, node-lib-v1:Label_ANT
- removed G-Logo: LOGO, node-lib-v1:Logo_GN-SE-4500px
- removed REF**: FabDrawing-4Layer, node-lib-v1:PCBStackup_FabDrawing-4Layer-Metric
- added G-GNSE: LOGO, node-lib-v1:Logo_GN_new_2000px, F.Cu at (148.4, 83.4)
- added L15: 8nH, Inductor_SMD:L_0402_1005Metric, F.Cu at (157.4, 88.9)
- C2: value 10nF -> DNM
- L13: value 23nH -> 27nH
- L14: value 4.3nH -> 6.5nH
- Q1: value CEN2321A -> PMV32UP,215
- Q2: value S9013W -> PMST4401,115
- R1: value 10K -> 0R
- U11: value ATECC608A-TNGLORA -> ATECC608B-TNGLORAU
- U2: value TPS3839G25 -> TPS3839G18DBZT‎
- U5: value STM32WLE5CC -> STM32WL55CCU6
- moved C7 65.2 mm to (147.8, 122.4), turned to 90 degrees
- moved C10 65.0 mm to (149.6, 120.2)
- moved C15 65.0 mm to (148.8, 115.3)
- moved C16 65.0 mm to (146.6, 112.1)
- moved C2 65.0 mm to (160.6, 132.9)
- moved C20 65.0 mm to (155.8, 105.7)
- moved C22 65.0 mm to (145.4, 108.0)
- moved C23 65.0 mm to (142.9, 111.6)
- moved C25 65.0 mm to (150.1, 100.8)
- moved C26 65.0 mm to (148.2, 100.8)
- moved C4 65.0 mm to (146.3, 124.4)
- moved C5 65.0 mm to (146.3, 126.5)
- moved F1 65.0 mm to (156.4, 128.2)
- moved G-FLASH 65.0 mm to (157.3, 115.1)
- moved G-version 65.0 mm to (162.6, 84.2)
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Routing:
- net GND: track 188.2 -> 198.1 mm, vias 493 -> 496
- net +BATT: track 13.8 -> 10.9 mm
- added copper zone on In1.Cu, net GND
- added copper zone on In2.Cu, net GND
- added copper zone on F.Cu, net Net-(C54-Pad1)
- added copper zone on F.Cu, net Net-(C54-Pad2)
- added copper zone on In2.Cu, net VDDRF
- removed copper zone on In1.LF, net GND
- removed copper zone on In2.PWR, net GND
- removed copper zone on F.Cu, net Net-(C55-Pad2)
- removed copper zone on In2.PWR, net VDDRF
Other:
- net class 100Ohm removed
- net class Default removed
- board text added: "1.8-5.5V"
- board text added: "868/915 MHz ANT"
- board text added: "genericnode.com"
- board text removed: "1. Material: 2. Soldermask color: 3. Silkscreen color: 4. Surface Finish: 5. Impedance Control: 6. VIAs: 7. Stackup:"
- board text removed: "2.5-5.5V"
- board text removed: "FR-4 (TG-150) Black/Blue White ENIG Yes Tented with soldermask See stackup table below for layer specific info"
- board text removed: "~PCB Specifications"
